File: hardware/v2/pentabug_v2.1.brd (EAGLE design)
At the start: 166.7 x 33 mm, 51 parts, among them IC1 ATMEGA88

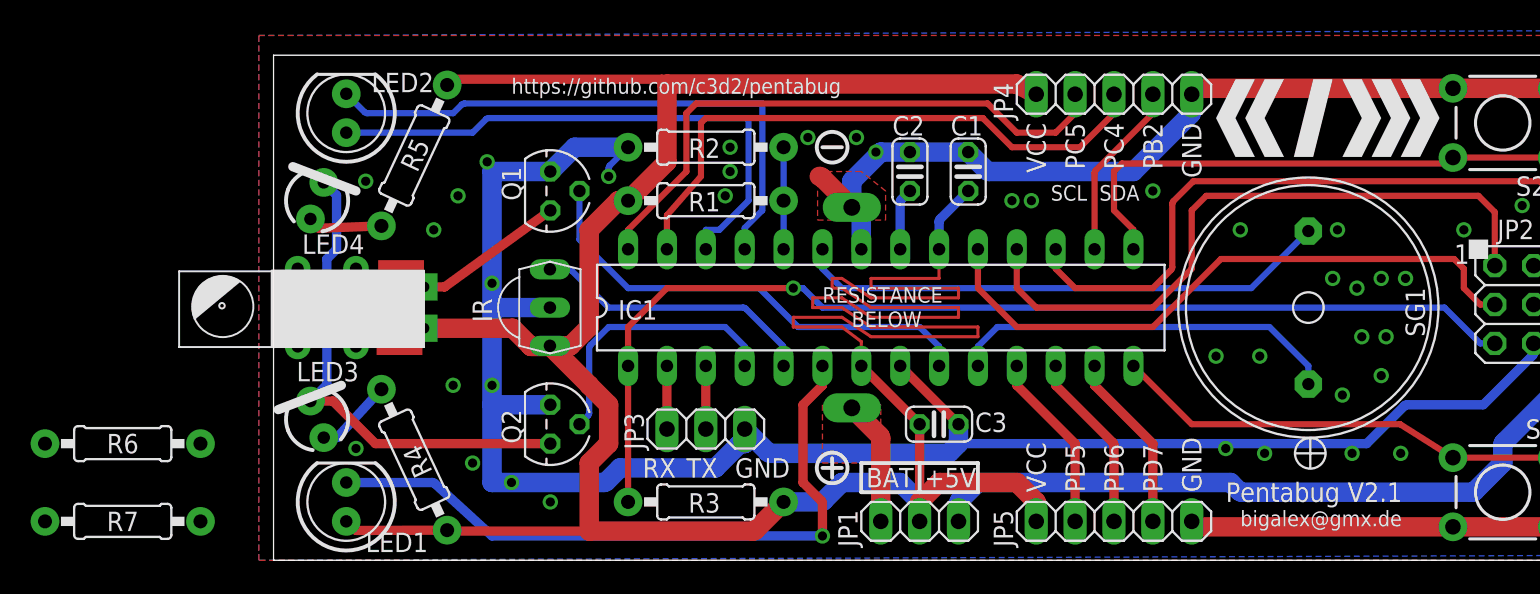
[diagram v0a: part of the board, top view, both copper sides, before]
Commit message: some improvent on placement of print and mounting holes for motor
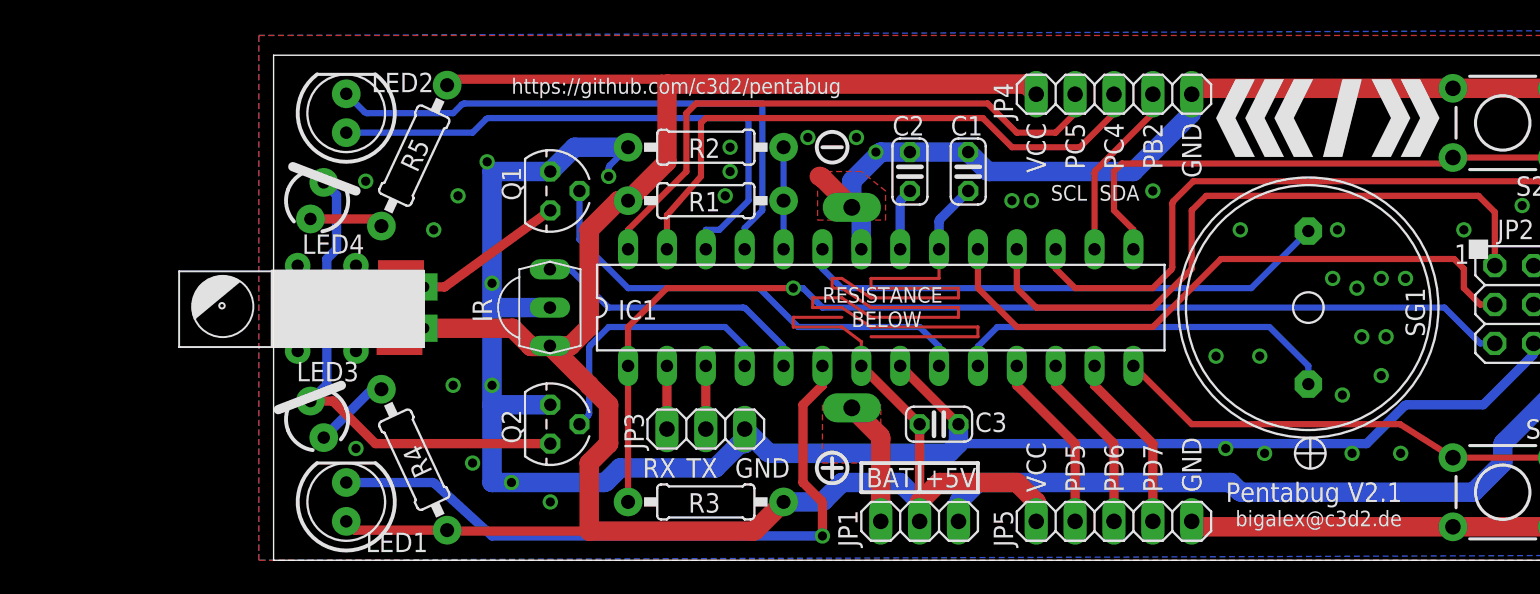
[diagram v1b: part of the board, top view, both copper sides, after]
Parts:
- removed R6: (no value), bigalexeasysolder:0207/10
- removed R7: 100K, bigalexeasysolder:0207/10
- IC1: value ATMEGA88 -> ATMEGA328P-PU
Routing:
- net VCC: track 225.7 -> 223.4 mm
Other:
- board text added: "bigalex@c3d2.de"
- board text removed: "bigalex@gmx.de"

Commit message: I can haz eazy solder transistors.
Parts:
- added SV1: (no value), con-lstb:MA05-2
- Q1, Q2: device transistors:TO-92 -> bigalexeasysolder:TO92-
- moved Q2 1.27 mm to (19.1, 7.62)
- moved Q1 1.27 mm to (19.1, 25.4)
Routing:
- net VCC: track 223.4 -> 237.1 mm
- net IRSEND: track 17.8 -> 20.1 mm
- net VIBRATE: track 30.8 -> 32.9 mm
- net N$3: track 36.9 -> 38.7 mm
- net N$5: track 37.9 -> 39.8 mm
- net N$11: track 32.2 -> 33.2 mm
- net GND: track 201.9 -> 201.0 mm, vias 39 -> 40
- net N$8: track 9.88 -> 10.4 mm

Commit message: moar easy soldering
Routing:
- net VCC: track 237.1 -> 219.3 mm
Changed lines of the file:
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@@
 <contactref element="JP5" pad="1"/>
 <wire x1="39.37" y1="12.7" x2="39.37" y2="14.2875" width="0.2032" layer="1"/>
-<wire x1="38.4175" y1="15.24" x2="27.305" y2="15.24" width="0.2032" layer="1"/>
-<wire x1="27.305" y1="15.24" x2="27.305" y2="15.875" width="0.2032" layer="1"/>
+<wire x1="38.4175" y1="15.24" x2="36.195" y2="15.24" width="0.2032" layer="1"/>
+<wire x1="36.195" y1="15.24" x2="36.195" y2="15.875" width="0.2032" layer="1"/>
 <wire x1="40.005" y1="14.605" x2="46.99" y2="14.605" width="0.2032" layer="1"/>
 <wire x1="46.99" y1="14.605" x2="46.99" y2="15.24" width="0.2032" layer="1"/>
@@
 <wire x1="21.5488" y1="14.0112" x2="21.59" y2="13.97" width="1.27" layer="1"/>
 <wire x1="39.37" y1="14.2875" x2="38.4175" y2="15.24" width="0.2032" layer="1"/>
-<wire x1="27.305" y1="15.875" x2="38.735" y2="15.875" width="0.2032" layer="1"/>
+<wire x1="36.195" y1="15.875" x2="38.735" y2="15.875" width="0.2032" layer="1"/>
 <wire x1="38.735" y1="15.875" x2="40.005" y2="14.605" width="0.2032" layer="1"/>
 <wire x1="40.64" y1="15.24" x2="39.37" y2="16.51" width="0.2032" layer="1"/>

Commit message: v2.1 production files, updated docs, some cleanup
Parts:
- removed LED10, LED11, LED12, LED13, LED14, LED15, LED16, LED17, LED18, LED5, LED6, LED7, LED8, LED9: (no value), led:LED5MM
- removed S3, S4, S5, S6, S7: (no value), switch-omron:B3F-10XX
- removed SV1: (no value), con-lstb:MA05-2
- removed SV4, SV5, SV__4, SV__5: (no value), con-lsta:FE05-1
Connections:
- removed net GND_L: SV__4.5, SV__5.5
- removed net GND_M: S3.3, S3.4, S4.3, S4.4, S5.3, S5.4, S6.3, S6.4, S7.3, S7.4, SV4.5, SV5.5
- removed net PB2_L: LED10.A, LED11.A, LED12.A, SV__5.4
- removed net PC4_L: LED13.A, LED14.A, LED15.A, SV__5.3
- removed net PC4_T: LED9.K, S7.1, S7.2, SV5.3
- removed net PC5_L: LED16.A, LED17.A, LED18.A, SV__5.2
- removed net PC5_T: LED8.K, S6.1, S6.2, SV5.2
- removed net PD5_L: LED10.K, LED13.K, LED16.K, SV__4.2
- removed net PD5_T: LED5.K, S3.1, S3.2, SV4.2
- removed net PD6_L: LED11.K, LED14.K, LED17.K, SV__4.3
- removed net PD6_T: LED6.K, S4.1, S4.2, SV4.3
- removed net PD7_L: LED12.K, LED15.K, LED18.K, SV__4.4
- removed net PD7_T: LED7.K, S5.1, S5.2, SV4.4
- removed net VCC_L: SV__4.1, SV__5.1
- removed net VCC_M: LED5.A, LED6.A, LED7.A, LED8.A, LED9.A, SV5.1
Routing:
- net VCC_M: track 43.8 -> 0.00 mm
- net PC4_T: track 35.3 -> 0.00 mm
- net PD5_L: track 35.1 -> 0.00 mm
- net PC5_L: track 30.8 -> 0.00 mm
- net VCC_L: track 27.9 -> 0.00 mm
- net PC5_T: track 27.6 -> 0.00 mm
- net PD5_T: track 27.4 -> 0.00 mm
- net PC4_L: track 26.7 -> 0.00 mm
- net PD6_L: track 26.2 -> 0.00 mm
- net PB2_L: track 25.1 -> 0.00 mm
- net PD6_T: track 24.1 -> 0.00 mm
- net PD7_L: track 24.0 -> 0.00 mm
- net PD7_T: track 21.6 -> 0.00 mm
- net GND_M: track 13.0 -> 0.00 mm
- net IRSEND: track 20.1 -> 20.6 mm
- removed copper zone on layer 1, net GND_L
- removed copper zone on layer 16, net GND_L
- removed copper zone on layer 1, net GND_M
- removed copper zone on layer 16, net GND_M
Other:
- board size 166.7 x 33 mm -> 86 x 33 mm
- board text removed: "2"
- board text removed: "3"
- board text removed: "4"
- board text removed: "5"
- board text removed: "for pentabug 2.0"
- board text removed: "ledmatrix"
- board text removed: "pentatonic"
